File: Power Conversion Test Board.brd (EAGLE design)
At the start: 136.7 x 125.3 mm, 54 parts, among them U1 LM2678, U2 LM2678

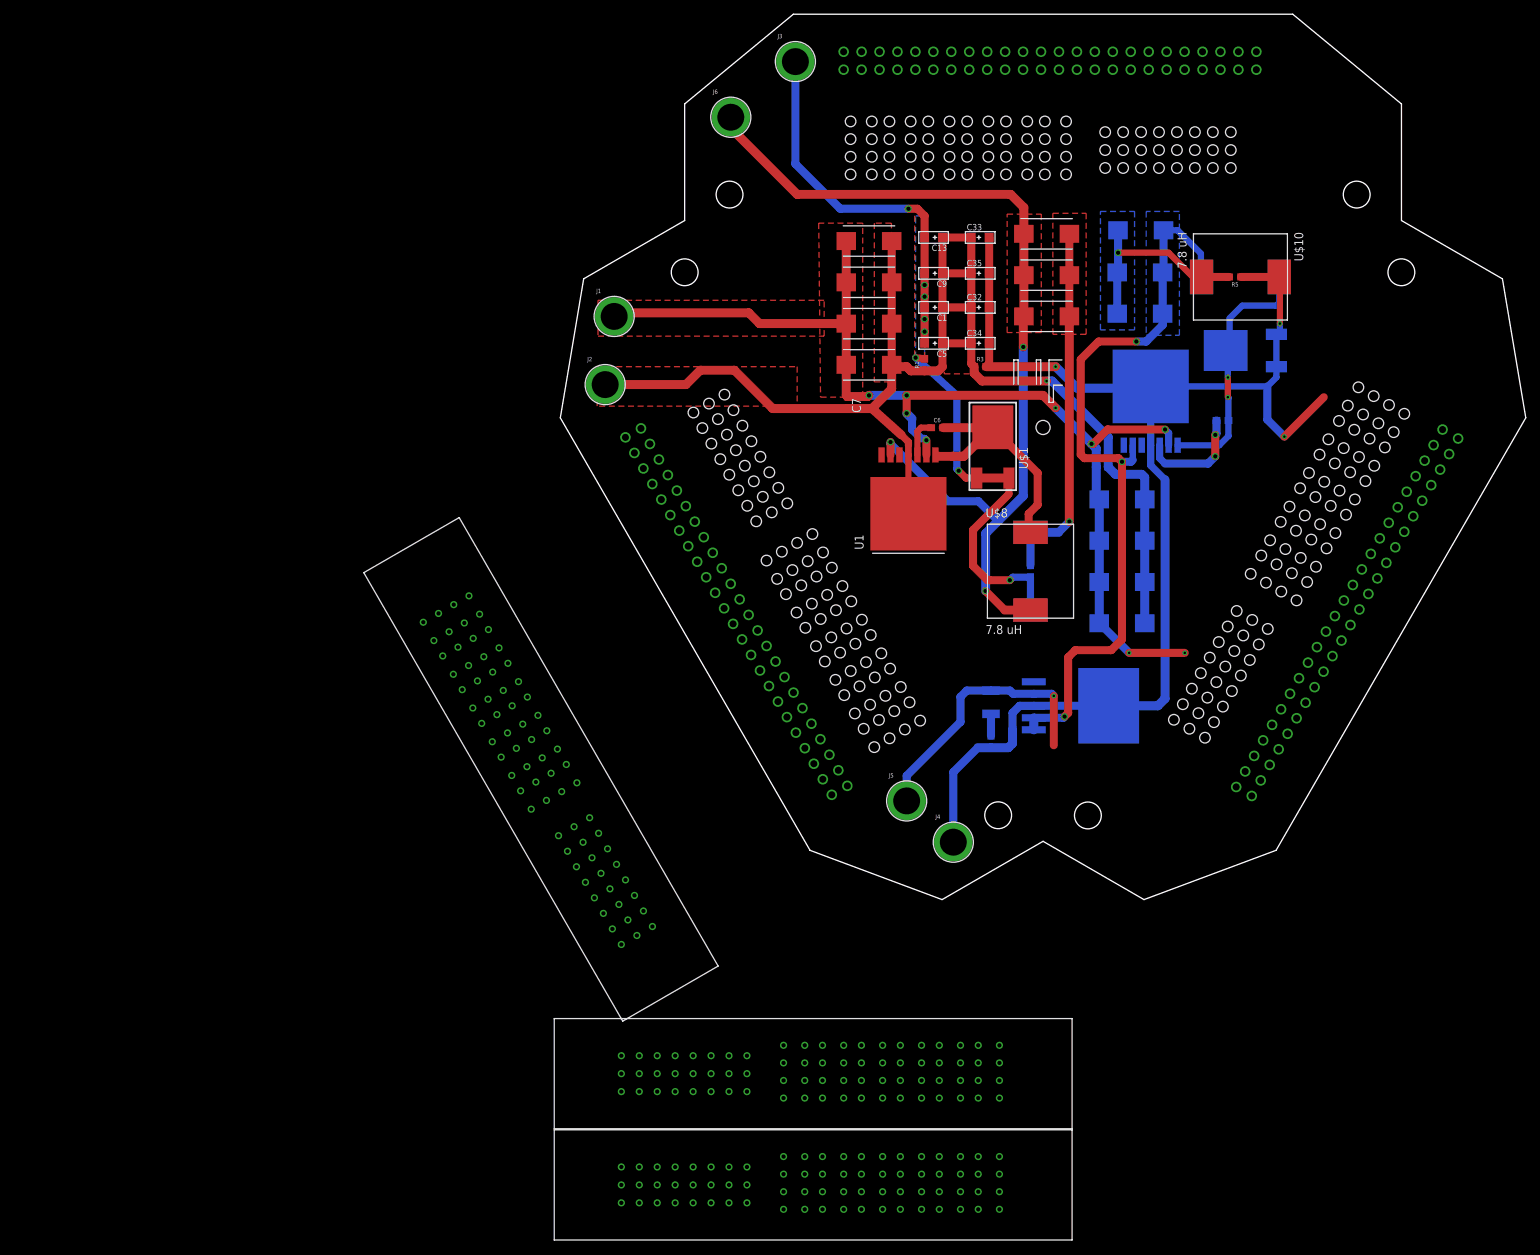
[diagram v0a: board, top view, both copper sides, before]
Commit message: Added the updated ET60S connectors
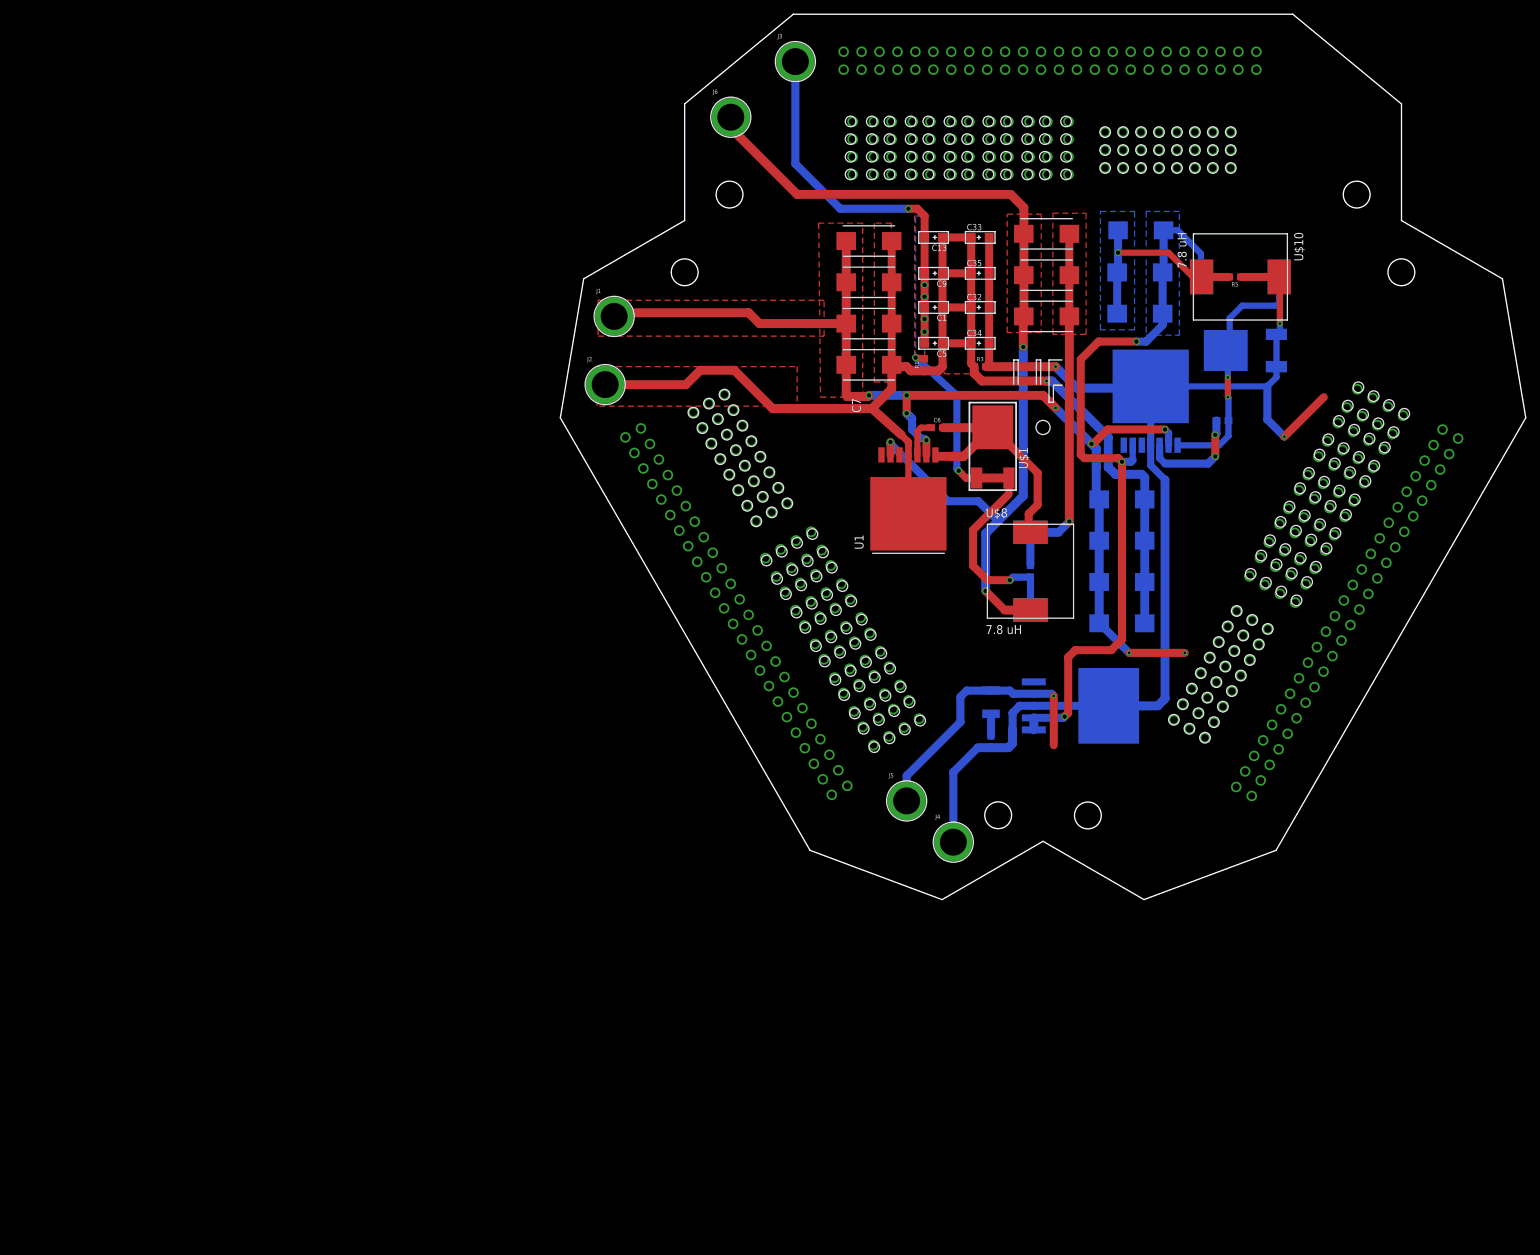
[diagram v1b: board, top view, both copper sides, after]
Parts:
- moved U$11 170.0 mm to (94.9, 108.6), flipped to the bottom
- moved U$6 94.1 mm to (91.3, 22.9), flipped to the bottom, turned to 120 degrees
- moved U$2 76.0 mm to (18.8, 69.0), flipped to the bottom, turned to 240 degrees

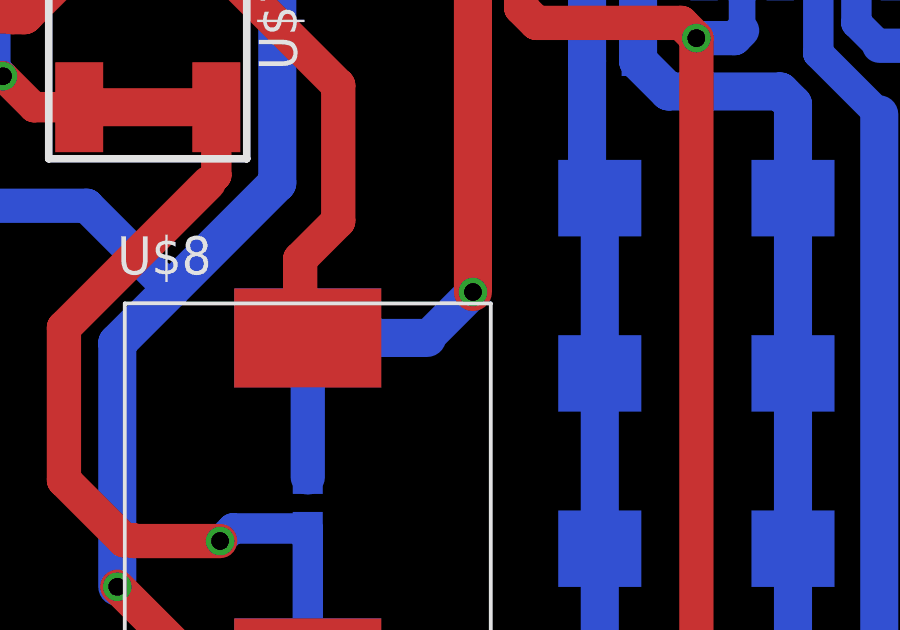
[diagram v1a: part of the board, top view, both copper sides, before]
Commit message: fixed a trace
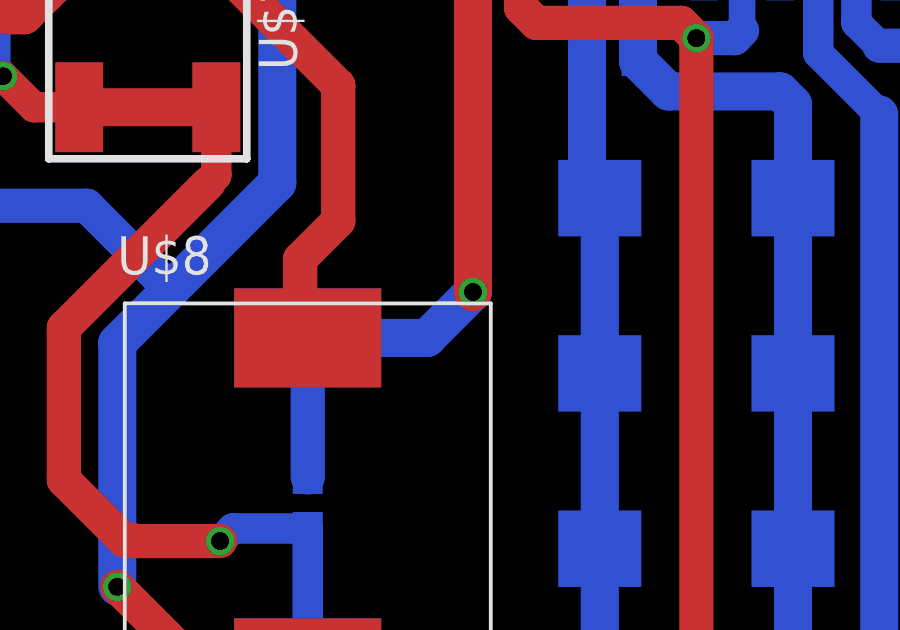
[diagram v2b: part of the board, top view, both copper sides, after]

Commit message: Changed stuff
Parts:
- removed U$11, U$2, U$6: ET60S, ET60S:ET60S
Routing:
- net 3.3VGND: track 188.9 -> 172.9 mm, vias 3 -> 2
- net +12V: track 156.5 -> 142.7 mm, vias 9 -> 7
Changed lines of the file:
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@@
 <?xml version="1.0" encoding="utf-8"?>
 <!DOCTYPE eagle SYSTEM "eagle.dtd">
-<eagle version="9.2.2">
+<eagle version="9.1.3">
 <drawing>
 <settings>
@@
 <element name="U$13" library="PDB_PCB_connectors" package="PDB_PCB" value="PDB_PCB_CONNEC" x="113.411" y="44.889940625" smashed="yes" rot="R330"/>
 <element name="U$14" library="PDB_PCB_connectors" package="PDB_PCB" value="PDB_PCB_CONNEC" x="74.041" y="119.126" smashed="yes" rot="R270"/>
-<element name="U$2" library="ET60S" package="ET60S" value="ET60S" x="18.837259375" y="68.95443125" smashed="yes" rot="MR240"/>
-<element name="U$6" library="ET60S" package="ET60S" value="ET60S" x="91.25564375" y="22.893115625" smashed="yes" rot="MR120"/>
-<element name="U$11" library="ET60S" package="ET60S" value="ET60S" x="94.8944" y="108.6358" smashed="yes" rot="MR0"/>
 </elements>
 <signals>
@@
 <vertex x="37.338" y="84.836"/>
 </polygon>
-<via x="88.392" y="34.925" extent="1-16" drill="0.35"/>
-<wire x1="88.392" y1="34.925" x2="80.518" y2="34.925" width="1.143" layer="1"/>
-<via x="80.518" y="34.925" extent="1-16" drill="0.35"/>
-<wire x1="80.518" y1="34.925" x2="76.327" y2="39.116" width="1.143" layer="16"/>
 <wire x1="76.327" y1="39.116" x2="76.282" y2="39.116" width="1.143" layer="16"/>
 <contactref element="U$12" pad="+12V17"/>
@@
 <wire x1="40.102" y1="117.475" x2="40.102" y2="120.015" width="0" layer="19" extent="1-1"/>
 <wire x1="40.468" y1="93.218" x2="40.102" y2="117.475" width="0" layer="19" extent="1-1"/>
-<wire x1="102.021603125" y1="26.940925" x2="88.392" y2="34.925" width="0" layer="19" extent="1-1"/>
+<wire x1="100.751603125" y1="24.741221875" x2="76.327" y2="39.116" width="0" layer="19" extent="16-16"/>
+<wire x1="102.021603125" y1="26.940925" x2="100.751603125" y2="24.741221875" width="0" layer="19" extent="1-1"/>
 <wire x1="104.22130625" y1="25.670925" x2="102.021603125" y2="26.940925" width="0" layer="19" extent="1-1"/>
 <wire x1="105.49130625" y1="27.87063125" x2="104.22130625" y2="25.670925" width="0" layer="19" extent="1-1"/>
@@
 <wire x1="104.561603125" y1="31.340334375" x2="106.76130625" y2="30.070334375" width="0" layer="19" extent="1-1"/>
 <wire x1="103.291603125" y1="29.14063125" x2="102.021603125" y2="26.940925" width="0" layer="19" extent="1-1"/>
-<wire x1="102.95130625" y1="23.471221875" x2="104.22130625" y2="25.670925" width="0" layer="19" extent="1-1"/>
+<wire x1="102.95130625" y1="23.471221875" x2="100.751603125" y2="24.741221875" width="0" layer="19" extent="1-1"/>
 <wire x1="101.68130625" y1="21.271515625" x2="102.95130625" y2="23.471221875" width="0" layer="19" extent="1-1"/>
-<wire x1="100.751603125" y1="24.741221875" x2="102.021603125" y2="26.940925" width="0" layer="19" extent="1-1"/>
-<wire x1="99.481603125" y1="22.541515625" x2="101.68130625" y2="21.271515625" width="0" layer="19" extent="1-1"/>
+<wire x1="99.481603125" y1="22.541515625" x2="100.751603125" y2="24.741221875" width="0" layer="19" extent="1-1"/>
 <wire x1="98.211603125" y1="20.3418125" x2="99.481603125" y2="22.541515625" width="0" layer="19" extent="1-1"/>
 <wire x1="100.41130625" y1="19.0718125" x2="101.68130625" y2="21.271515625" width="0" layer="19" extent="1-1"/>
@@
 <wire x1="55.626" y1="18.034" x2="55.626" y2="8.128" width="1.143" layer="16"/>
 <wire x1="59.094" y1="21.502" x2="55.626" y2="18.034" width="1.143" layer="16"/>
-<via x="102.489" y="65.532" extent="1-16" drill="0.35"/>
-<wire x1="102.489" y1="65.532" x2="100.076" y2="67.945" width="1.143" layer="16"/>
-<wire x1="100.076" y1="72.644" x2="100.076" y2="67.945" width="1.143" layer="16"/>
-<wire x1="108.068465625" y1="71.111465625" x2="102.489" y2="65.532" width="1.143" layer="1"/>
 </signal>
 <signal name="N$10">

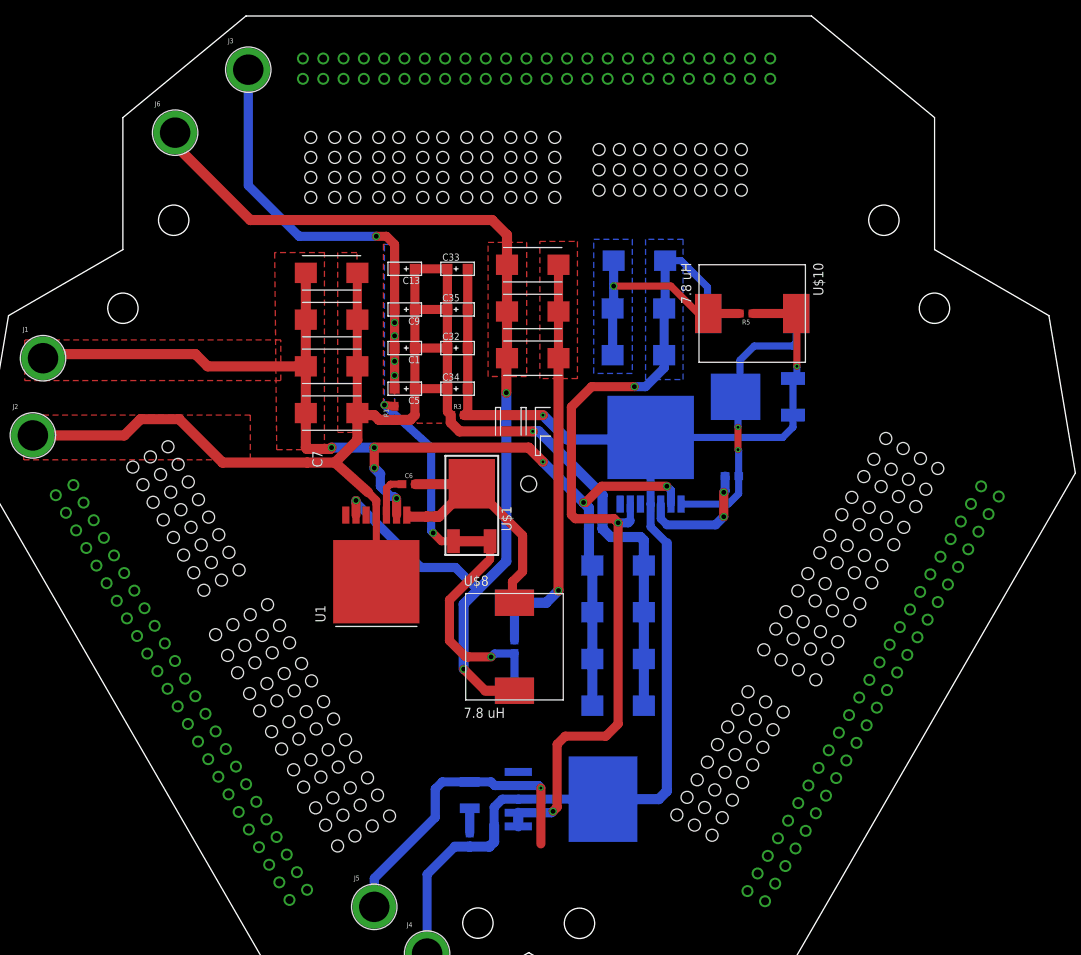
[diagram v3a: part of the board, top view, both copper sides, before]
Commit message: Replaced connectors
the ones to the distribution board
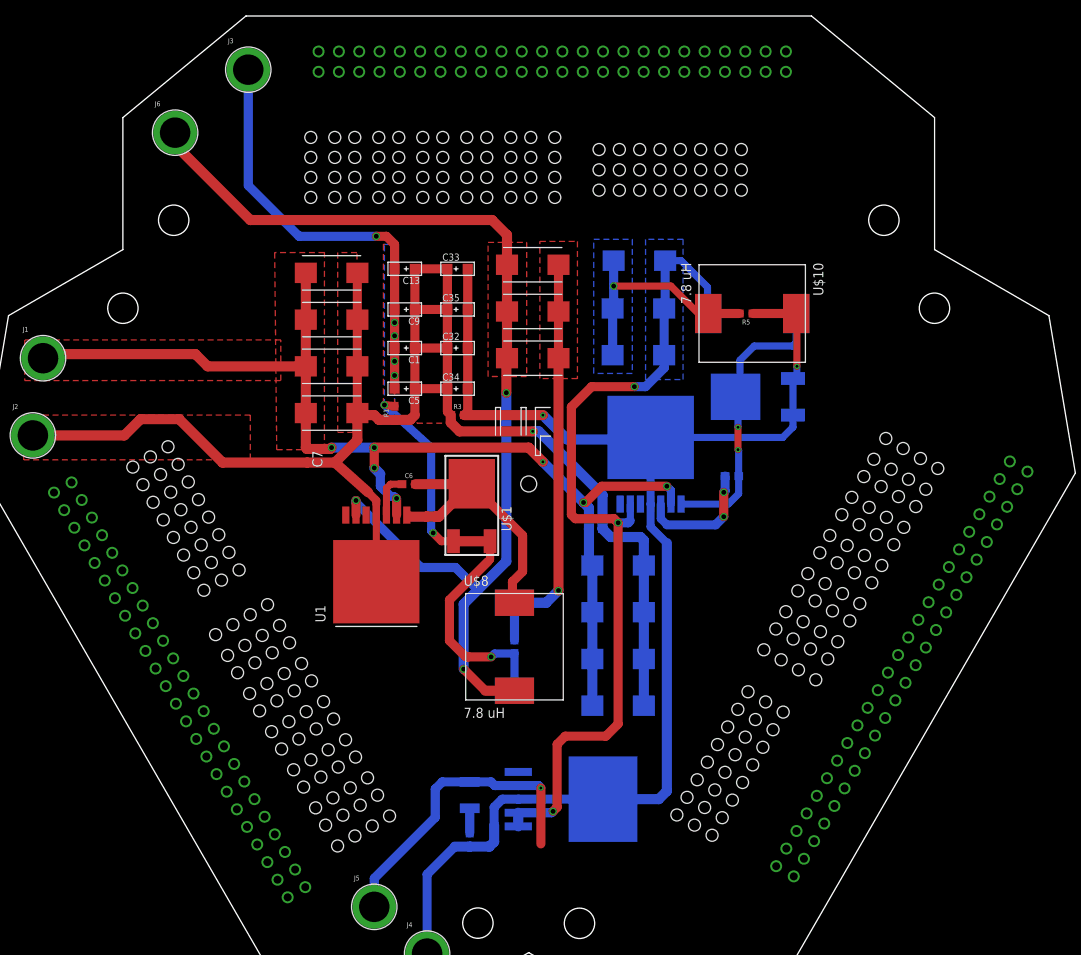
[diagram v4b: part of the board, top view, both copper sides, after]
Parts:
- moved U$13 4.75 mm to (117.0, 48.0)
- moved U$14 2.15 mm to (76.0, 120.0)
- moved U$12 0.40 mm to (22.0, 45.0)

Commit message: Made some minor changes to the board, just uploading for saving purposes
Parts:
- removed R2, R5: 0, SparkFun-Resistors:0603
- removed U$12, U$13, U$14: PDB_PCB_CONNEC, PDB_PCB_connectors:PDB_PCB
- added R6, R7: 0, audio amplifier example:R1206
- added U$2: PDB_PCB_CONNEC, PDB_PCB_connectors:PDB_PCB_2
- moved C20 7.49 mm to (99.0, 62.5), turned to 90 degrees
- moved U$3 5.99 mm to (102.1, 74.2)
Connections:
- net +12V: now also U$2.+12V1, U$2.+12V10, U$2.+12V11, U$2.+12V12, U$2.+12V13, U$2.+12V14, U$2.+12V15, U$2.+12V16, U$2.+12V17, U$2.+12V18, U$2.+12V19, U$2.+12V2, U$2.+12V20, U$2.+12V21, U$2.+12V22, U$2.+12V23, U$2.+12V24, U$2.+12V25, U$2.+12V26, U$2.+12V27, U$2.+12V28, U$2.+12V29, U$2.+12V3, U$2.+12V30, U$2.+12V31, U$2.+12V32, U$2.+12V33, U$2.+12V34, U$2.+12V35, U$2.+12V36, U$2.+12V37, U$2.+12V38, U$2.+12V39, U$2.+12V4, U$2.+12V40, U$2.+12V41, U$2.+12V42, U$2.+12V43, U$2.+12V44, U$2.+12V45, U$2.+12V46, U$2.+12V47, U$2.+12V48, U$2.+12V49, U$2.+12V5, U$2.+12V50, U$2.+12V51, U$2.+12V52, U$2.+12V53, U$2.+12V54, U$2.+12V55, U$2.+12V56, U$2.+12V57, U$2.+12V58, U$2.+12V59, U$2.+12V6, U$2.+12V60, U$2.+12V61, U$2.+12V62, U$2.+12V63, U$2.+12V64, U$2.+12V65, U$2.+12V66, U$2.+12V67, U$2.+12V68, U$2.+12V69, U$2.+12V7, U$2.+12V70, U$2.+12V71, U$2.+12V72, U$2.+12V8, U$2.+12V9; no longer U$12.+12V1, U$12.+12V10, U$12.+12V11, U$12.+12V12, U$12.+12V13, U$12.+12V14, U$12.+12V15, U$12.+12V16, U$12.+12V17, U$12.+12V18, U$12.+12V19, U$12.+12V2, U$12.+12V20, U$12.+12V21, U$12.+12V22, U$12.+12V23, U$12.+12V24, U$12.+12V3, U$12.+12V4, U$12.+12V5, U$12.+12V6, U$12.+12V7, U$12.+12V8, U$12.+12V9, U$13.+12V1, U$13.+12V10, U$13.+12V11, U$13.+12V12, U$13.+12V13, U$13.+12V14, U$13.+12V15, U$13.+12V16, U$13.+12V17, U$13.+12V18, U$13.+12V19, U$13.+12V2, U$13.+12V20, U$13.+12V21, U$13.+12V22, U$13.+12V23, U$13.+12V24, U$13.+12V3, U$13.+12V4, U$13.+12V5, U$13.+12V6, U$13.+12V7, U$13.+12V8, U$13.+12V9, U$14.+12V1, U$14.+12V10, U$14.+12V11, U$14.+12V12, U$14.+12V13, U$14.+12V14, U$14.+12V15, U$14.+12V16, U$14.+12V17, U$14.+12V18, U$14.+12V19, U$14.+12V2, U$14.+12V20, U$14.+12V21, U$14.+12V22, U$14.+12V23, U$14.+12V24, U$14.+12V3, U$14.+12V4, U$14.+12V5, U$14.+12V6, U$14.+12V7, U$14.+12V8, U$14.+12V9
- net 3.3VGND: now also R6.1; no longer R5.1
- net 5VGND: now also R7.1; no longer R2.1
- net GND: now also U$2.GND1, U$2.GND10, U$2.GND11, U$2.GND12, U$2.GND13, U$2.GND14, U$2.GND15, U$2.GND16, U$2.GND17, U$2.GND18, U$2.GND19, U$2.GND2, U$2.GND20, U$2.GND21, U$2.GND22, U$2.GND23, U$2.GND24, U$2.GND25, U$2.GND26, U$2.GND27, U$2.GND28, U$2.GND29, U$2.GND3, U$2.GND30, U$2.GND31, U$2.GND32, U$2.GND33, U$2.GND34, U$2.GND35, U$2.GND36, U$2.GND37, U$2.GND38, U$2.GND39, U$2.GND4, U$2.GND40, U$2.GND41, U$2.GND42, U$2.GND43, U$2.GND44, U$2.GND45, U$2.GND46, U$2.GND47, U$2.GND48, U$2.GND49, U$2.GND5, U$2.GND50, U$2.GND51, U$2.GND52, U$2.GND53, U$2.GND54, U$2.GND55, U$2.GND56, U$2.GND57, U$2.GND58, U$2.GND59, U$2.GND6, U$2.GND60, U$2.GND61, U$2.GND62, U$2.GND63, U$2.GND64, U$2.GND65, U$2.GND66, U$2.GND67, U$2.GND68, U$2.GND69, U$2.GND7, U$2.GND70, U$2.GND71, U$2.GND72, U$2.GND8, U$2.GND9; no longer U$12.GND10, U$12.GND11, U$12.GND12, U$12.GND13, U$12.GND14, U$12.GND15, U$12.GND16, U$12.GND17, U$12.GND18, U$12.GND19, U$12.GND2, U$12.GND20, U$12.GND21, U$12.GND22, U$12.GND23, U$12.GND24, U$12.GND3, U$12.GND4, U$12.GND5, U$12.GND6, U$12.GND7, U$12.GND8, U$12.GND9, U$13.GND10, U$13.GND11, U$13.GND12, U$13.GND13, U$13.GND14, U$13.GND15, U$13.GND16, U$13.GND17, U$13.GND18, U$13.GND19, U$13.GND2, U$13.GND20, U$13.GND21, U$13.GND22, U$13.GND23, U$13.GND24, U$13.GND3, U$13.GND4, U$13.GND5, U$13.GND6, U$13.GND7, U$13.GND8, U$13.GND9, U$14.GND10, U$14.GND11, U$14.GND12, U$14.GND13, U$14.GND14, U$14.GND15, U$14.GND16, U$14.GND17, U$14.GND18, U$14.GND19, U$14.GND2, U$14.GND20, U$14.GND21, U$14.GND22, U$14.GND23, U$14.GND24, U$14.GND3, U$14.GND4, U$14.GND5, U$14.GND6, U$14.GND7, U$14.GND8, U$14.GND9
- net N$4: now also R6.2; no longer R5.2
- net N$8: now also R7.2; no longer R2.2
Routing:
- net 3.3VGND: track 172.9 -> 186.6 mm, vias 2 -> 3
- net N$7: track 36.6 -> 44.0 mm, vias 2 -> 0
- net 5VGND: track 109.7 -> 103.2 mm, vias 8 -> 7
- net N$2: track 15.6 -> 16.4 mm, vias 2 -> 0
